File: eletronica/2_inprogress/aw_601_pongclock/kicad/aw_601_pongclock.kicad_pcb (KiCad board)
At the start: 2 copper layers, 149.9 x 199.4 mm, 91 parts, among them CON1 BARREL_JACK, IC1 ATMEGA8-P, Q1 2N3904G, Q10 2N3904G, Q11 2N3904G, Q12 2N3904G, Q13 2N3904G, Q14 2N3904G, Q15 2N3904G, Q16 2N3904G, Q17 2N3904G, Q18 2N3904G, Q19 2N3904G, Q2 2N3904G, Q20 2N3904G, Q21 2N3904G, Q22 2N3904G, Q23 2N3904G, Q24 2N3904G, Q25 2N3904G, Q26 2N3904G, Q27 2N3904G, Q28 2N3904G, Q29 2N3904G, Q3 2N3904G, Q30 2N3904G, Q31 2N3904G, Q32 2N3904G, Q4 2N3904G, Q5 2N3904G, Q6 2N3904G, Q7 2N3904G, Q8 2N3904G, Q9 2N3904G, SW1 SW_PUSH, SW2 SW_PUSH, SW3 SW_PUSH, SW4 SW_PUSH, U1 4514, U2 ULN2803, U3 ULN2803, U4 ULN2803, U5 ULN2803, U6 74HC4094, U7 74HC4094, U8 74HC4094, U9 74HC4094, X1 16Mhz

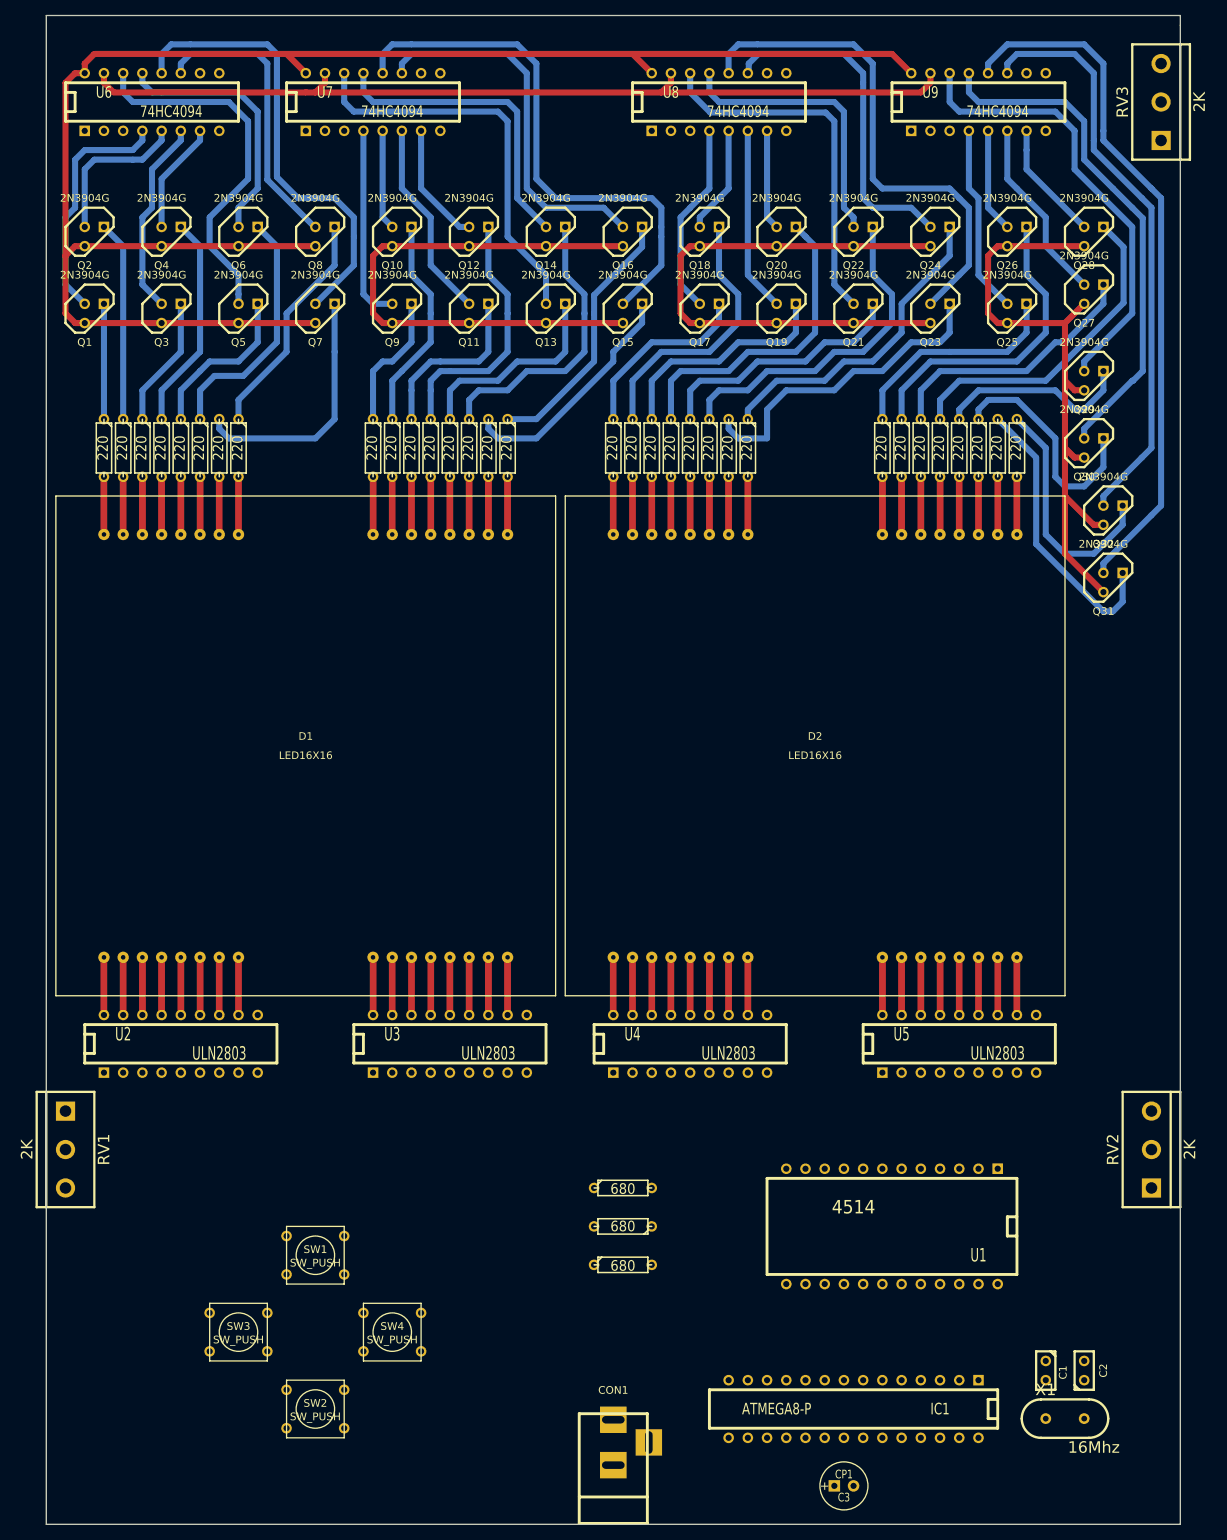
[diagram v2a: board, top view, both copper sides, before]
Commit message: 
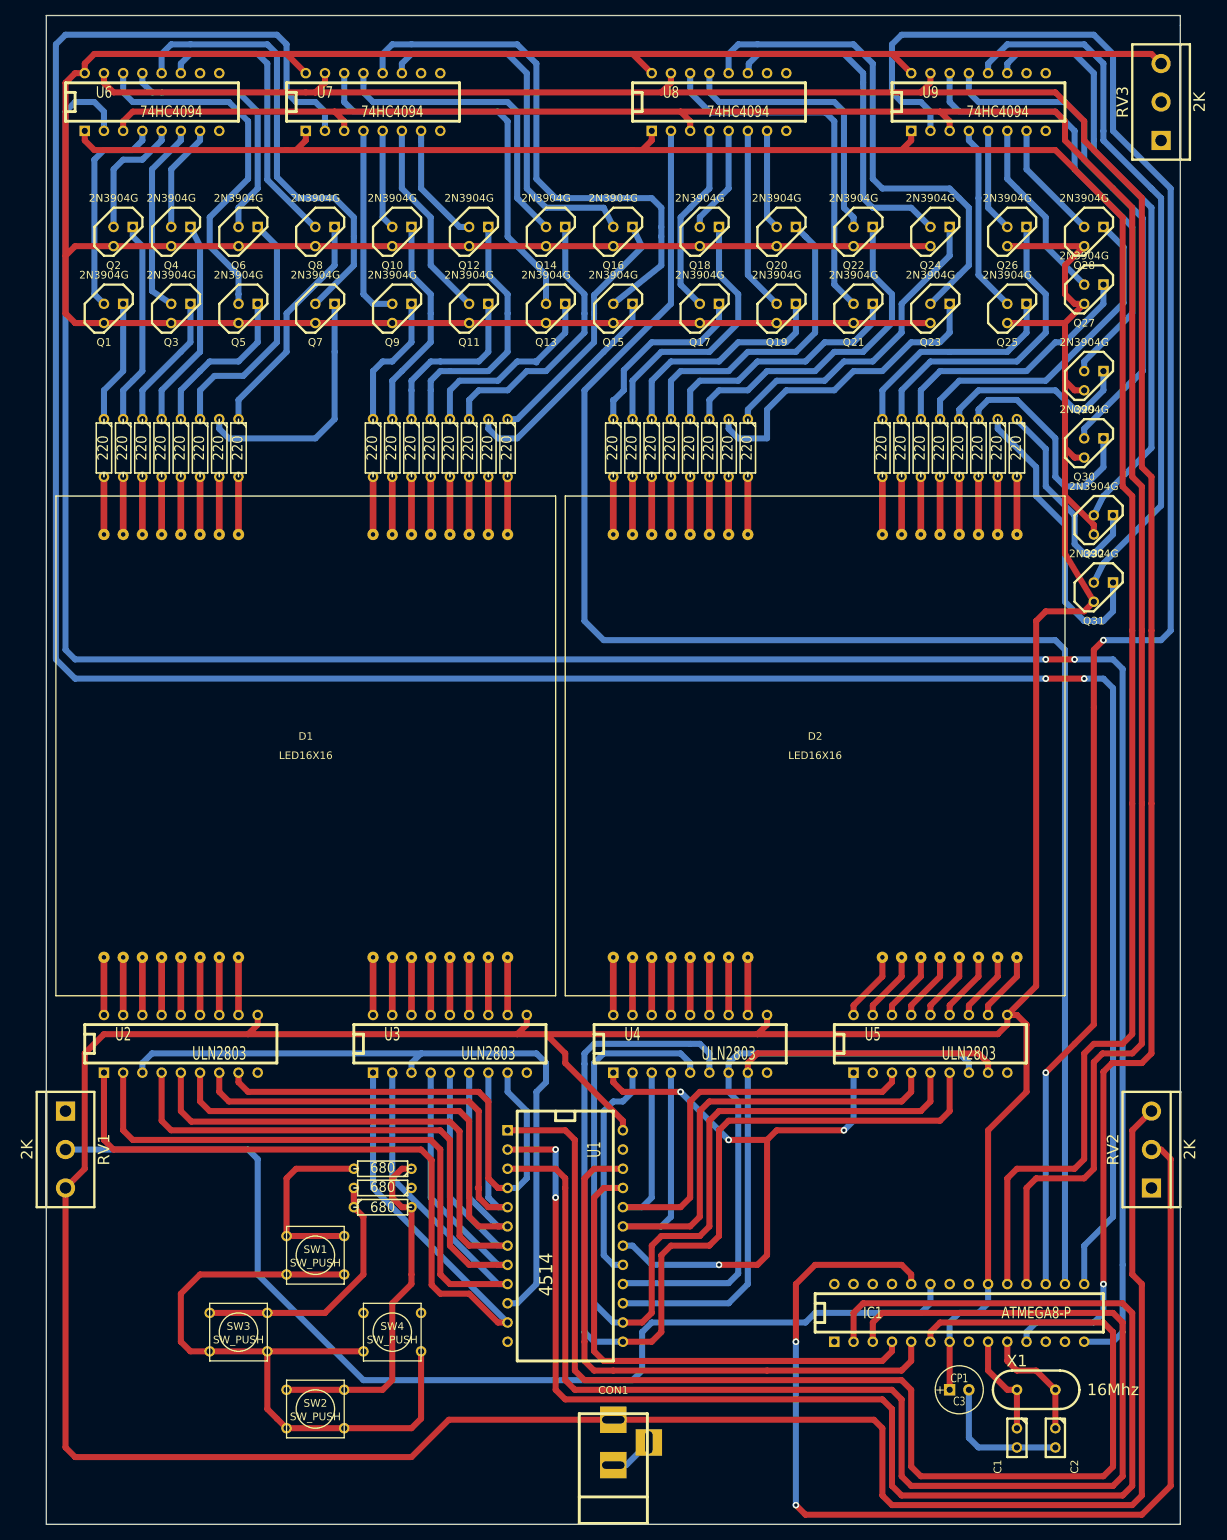
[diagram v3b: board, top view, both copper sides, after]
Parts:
- moved U1 43.2 mm to (104.1, 199.4), turned to 270 degrees
- moved R1 34.2 mm to (80.0, 190.5), turned to 180 degrees
- moved R2 31.9 mm to (80.0, 195.6), turned to 0 degrees
- moved R3 31.8 mm to (80.0, 193.0), turned to 180 degrees
- moved C3 19.8 mm to (156.2, 219.7)
- moved IC1 18.9 mm to (156.2, 209.6), turned to 0 degrees
- moved C2 9.67 mm to (168.9, 226.1), turned to 270 degrees
- moved C1 9.67 mm to (163.8, 226.1)
- moved X1 5.39 mm to (166.4, 219.7)
- moved Q2 3.81 mm to (45.7, 67.3)
- moved U5 3.81 mm to (152.4, 174.0)
- moved Q1 2.54 mm to (44.5, 77.5)
- moved Q31 1.80 mm to (175.3, 114.3)
- moved Q32 1.80 mm to (175.3, 105.4)
- moved Q3 1.27 mm to (53.3, 77.5)
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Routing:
- net +5V: track 454.9 -> 1032.0 mm
- net /DATA1: track 0.00 -> 349.4 mm, vias 0 -> 2
- net /DATA0: track 0.00 -> 313.8 mm, vias 0 -> 2
- net /STR: track 0.00 -> 306.9 mm
- net /CP: track 0.00 -> 306.2 mm
- net /DATA3: track 0.00 -> 222.8 mm, vias 0 -> 2
- net /DATA2: track 0.00 -> 218.4 mm
- net /OE: track 118.9 -> 320.7 mm, vias 0 -> 1
- net /D1: track 0.00 -> 191.1 mm, vias 0 -> 2
- net /D2: track 0.00 -> 177.7 mm
- net /STRB: track 0.00 -> 167.5 mm
- net N-00000111: track 0.00 -> 145.6 mm
- net N-00000110: track 0.00 -> 145.2 mm, vias 0 -> 2
- net N-0000040: track 0.00 -> 137.6 mm
- net N-0000063: track 0.00 -> 122.3 mm
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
